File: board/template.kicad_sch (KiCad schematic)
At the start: 7 parts, among them J1 USB4081-03-A, Q1 NTTFS5C673NLTAG, Q2 NTTFS5C673NLTAG, U1 APK43070DKZ-13-FA01

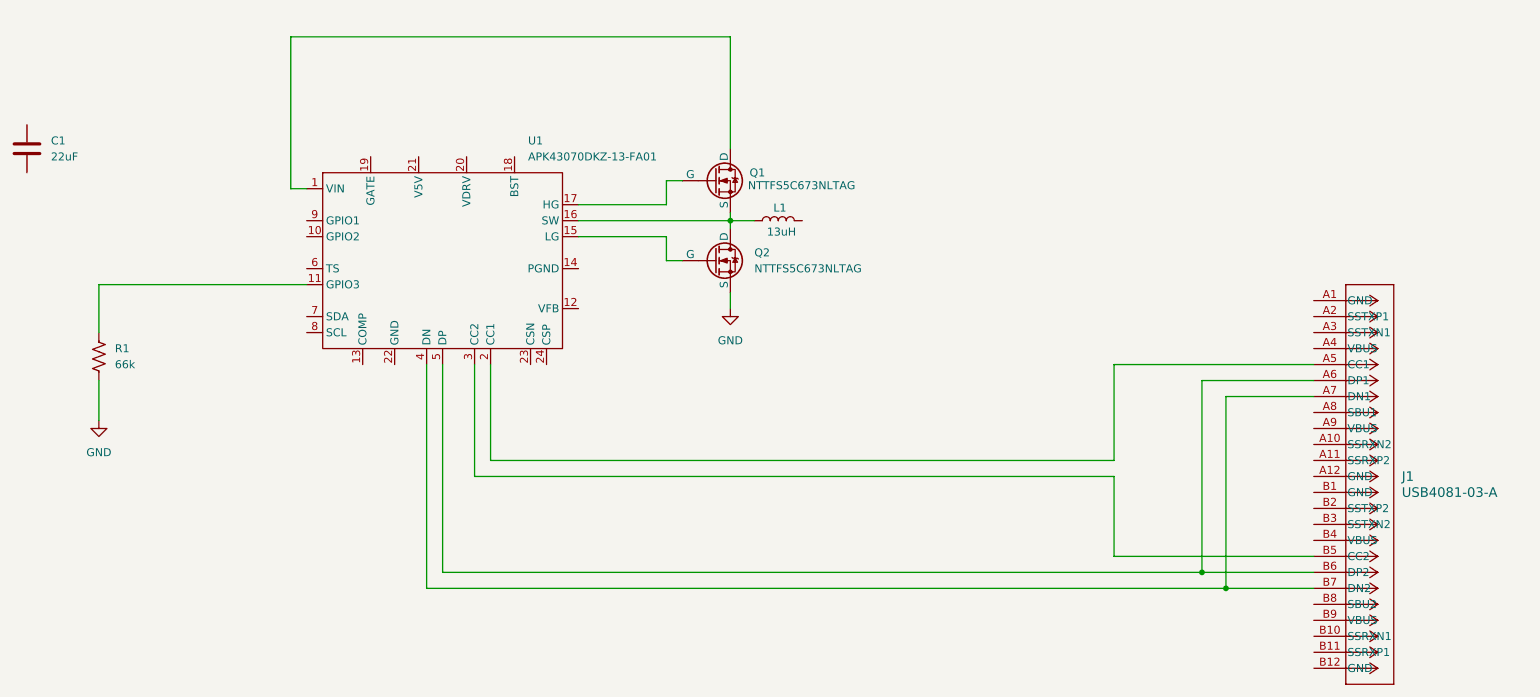
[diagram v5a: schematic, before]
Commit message: Configured GPIO pins
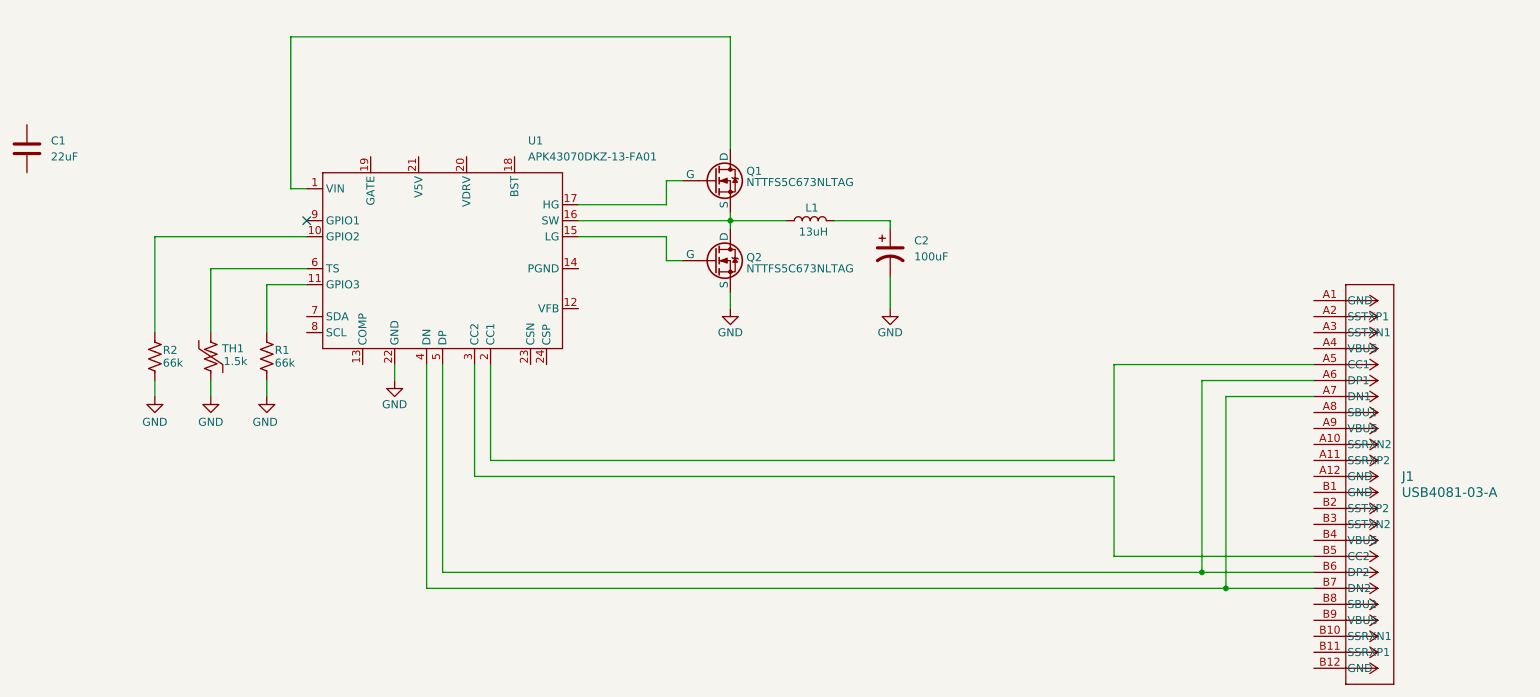
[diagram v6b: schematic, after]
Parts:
- added C2: 100uF, symbol Device:C_Polarized_US
- added R2: 66k, symbol Device:R_US
- added TH1: 1.5k, symbol Device:Thermistor_US
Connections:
- net GND: now also U1.22 (GND), C2.2, R2.2, TH1.2
- net at U1.10 (GPIO2): now also R2.1
- net at U1.6 (TS): now also TH1.1
- net at L1.2: now also C2.1
- no-connect marks 0 -> 1
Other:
- moved on the sheet: L1, R1
